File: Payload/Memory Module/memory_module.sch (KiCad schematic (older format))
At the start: 12 parts

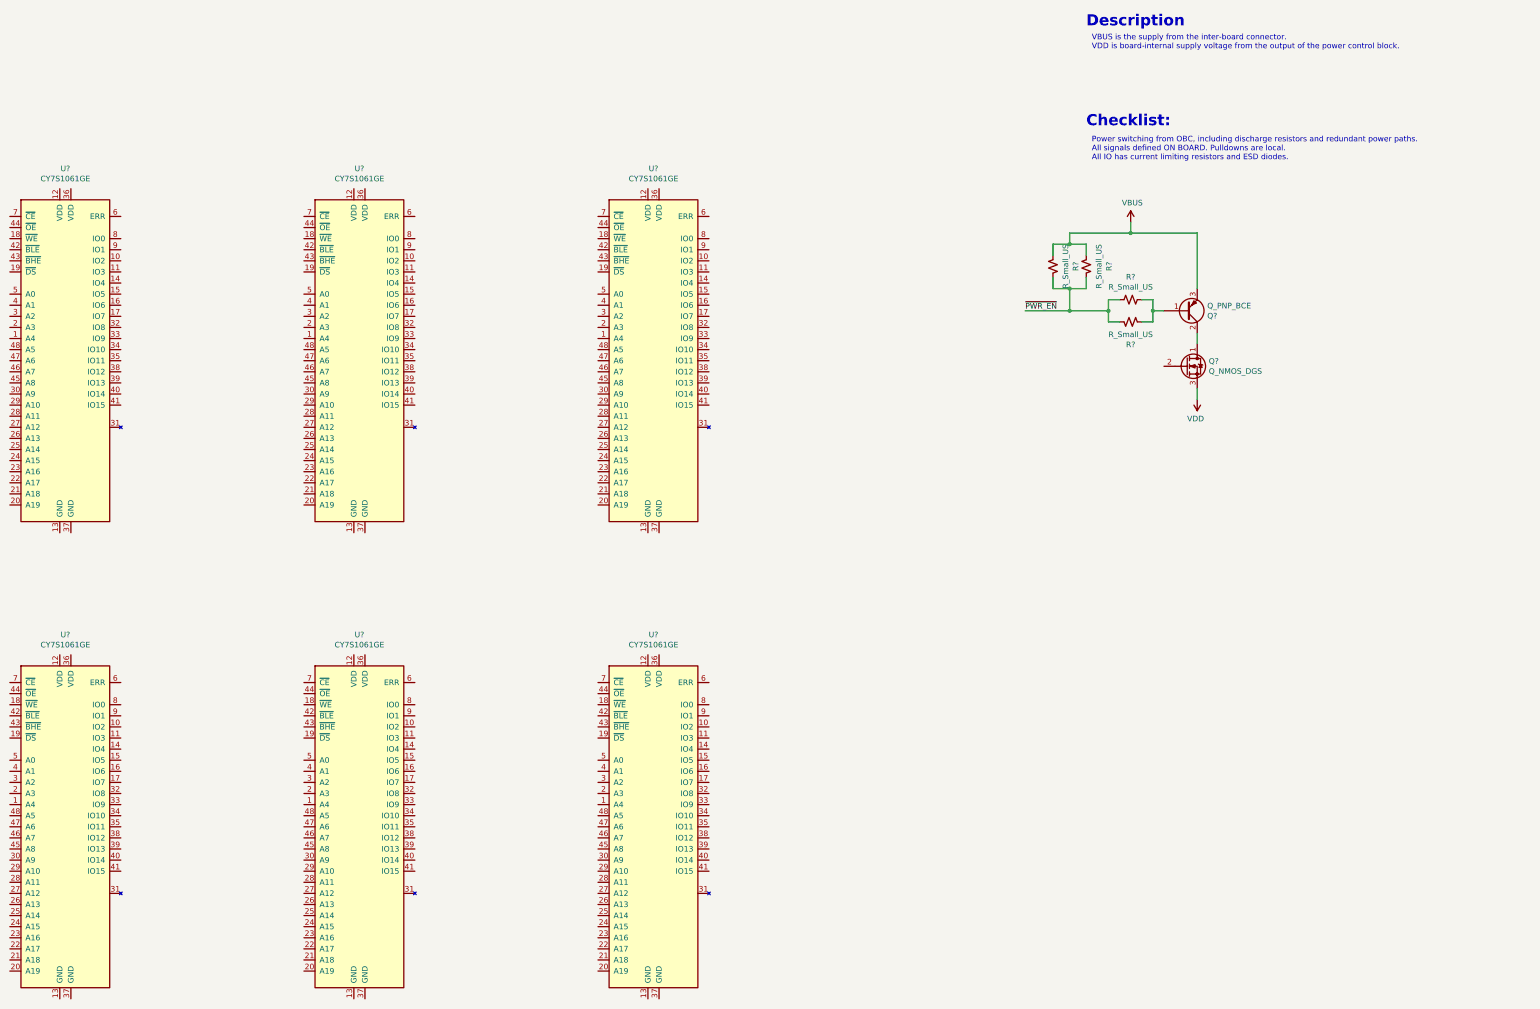
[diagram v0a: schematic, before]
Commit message: Work on inter-board connectors
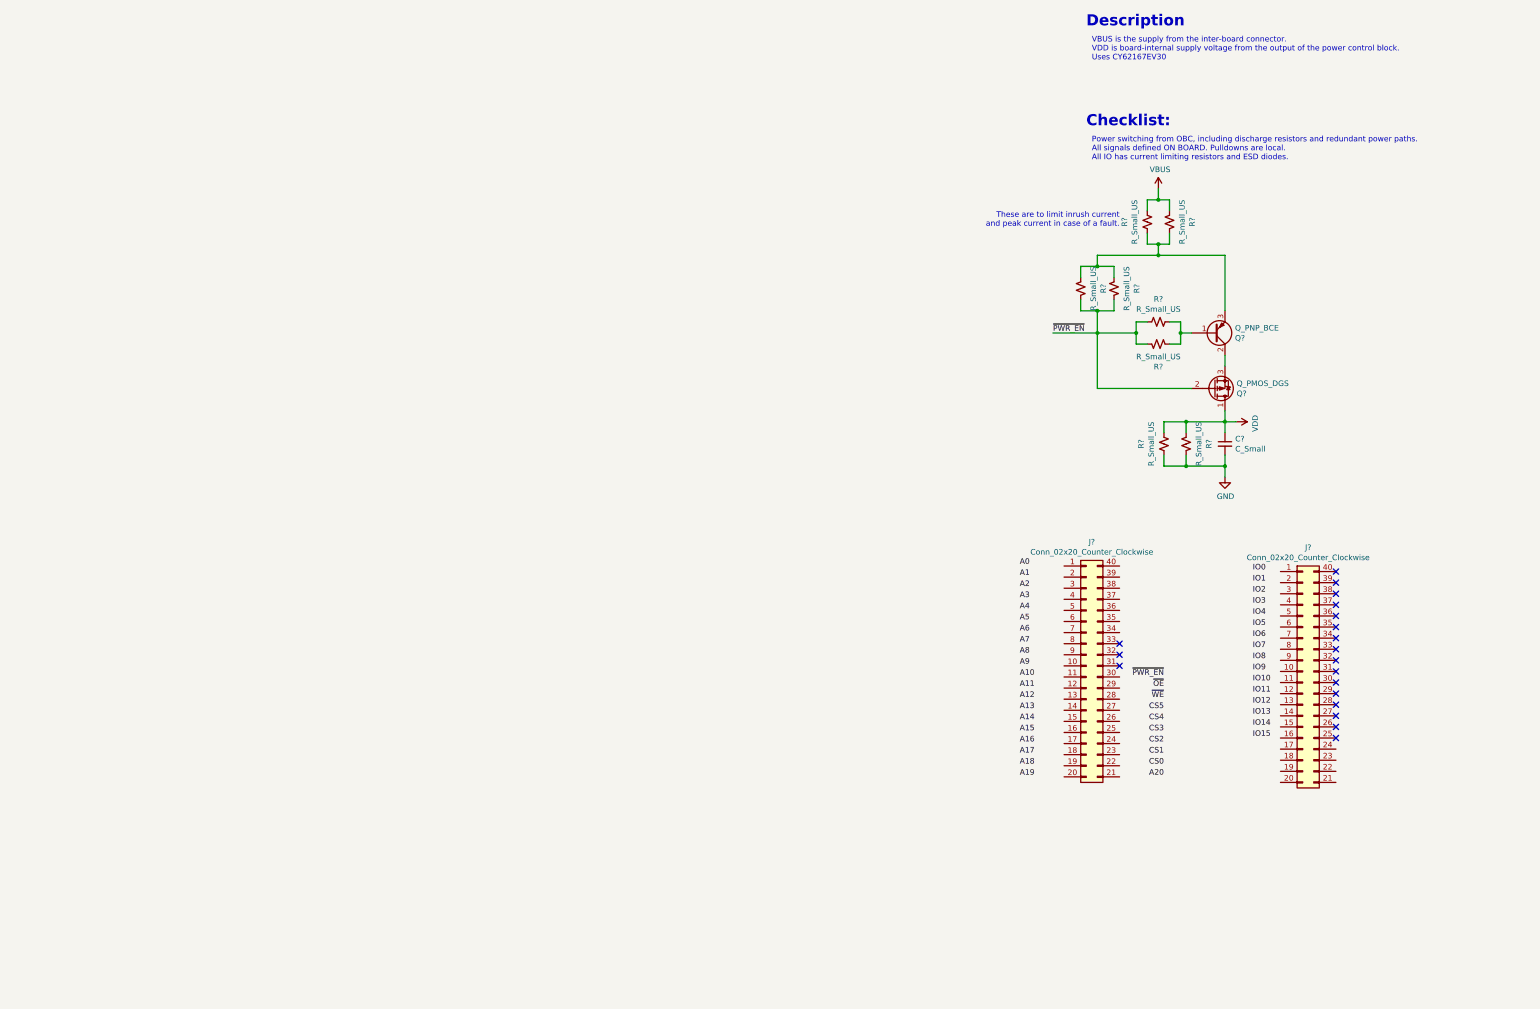
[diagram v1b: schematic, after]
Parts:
- removed Q?: Q_NMOS_DGS, symbol Device:Q_NMOS_DGS
- removed U? (x6): CY7S1061GE, Package_SO:TSOP-I-48_18.4x12mm_P0.5mm, symbol Payload2:CY7S1061GE
- added C?: C_Small, symbol Device:C_Small
- added J? (x2): Conn_02x20_Counter_Clockwise, symbol Connector_Generic:Conn_02x20_Counter_Clockwise
- added Q?: Q_PMOS_DGS, symbol Device:Q_PMOS_DGS
- added R? (x4): R_Small_US, symbol Device:R_Small_US
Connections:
- net VBUS: now also R?.1, R?.1; no longer Q?.3 (E), R?.1, R?.1
- net VDD: now also C?.1, Q?.1 (D), R?.1, R?.1
- net ~PWR_EN: now also Q?.2 (G)
- net at Q?.2 (C): now also Q?.3 (S)
- new net: Q?.3 (E), R?.1, R?.1, R?.2, R?.2
- new net GND: C?.2, R?.2, R?.2
- no-connect marks 0 -> 19
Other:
- note added: "These are to limit inrush current\nand peak current in case of a fault."
- note added: "VBUS is the supply from the inter-board connector.\nVDD is board-internal supply voltage from the output of the power control block.\nUses CY62167EV30"
- note removed: "VBUS is the supply from the inter-board connector.\nVDD is board-internal supply voltage from the output of the power control block."
- moved on the sheet: Q?, R?
